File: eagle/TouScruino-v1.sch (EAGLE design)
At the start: 42 parts, among them J1 AVR_ISP, Q1 8MHz, Q2 MMBT2222A, Q3 8MHz, U1 ATMEGA1284P, U2 PJ28004C, U3 ARDUINO_SHIELD, U4 MCP73831, U5 MIC5209-3.3YS, X1 USBSMD

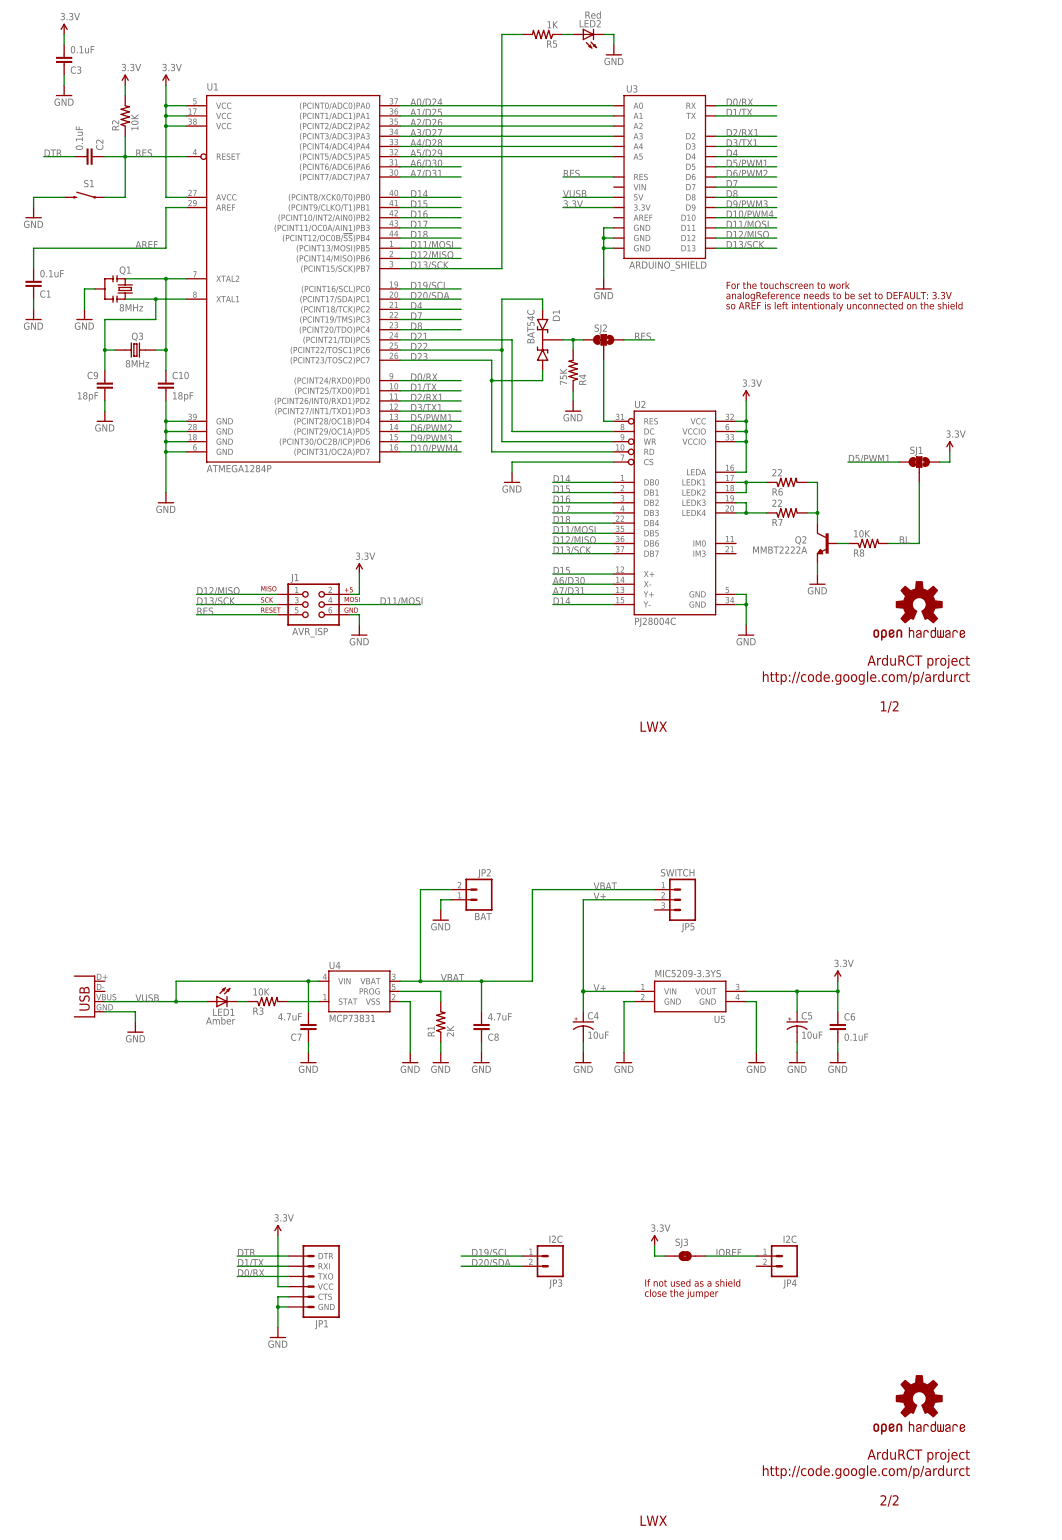
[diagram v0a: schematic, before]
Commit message: 
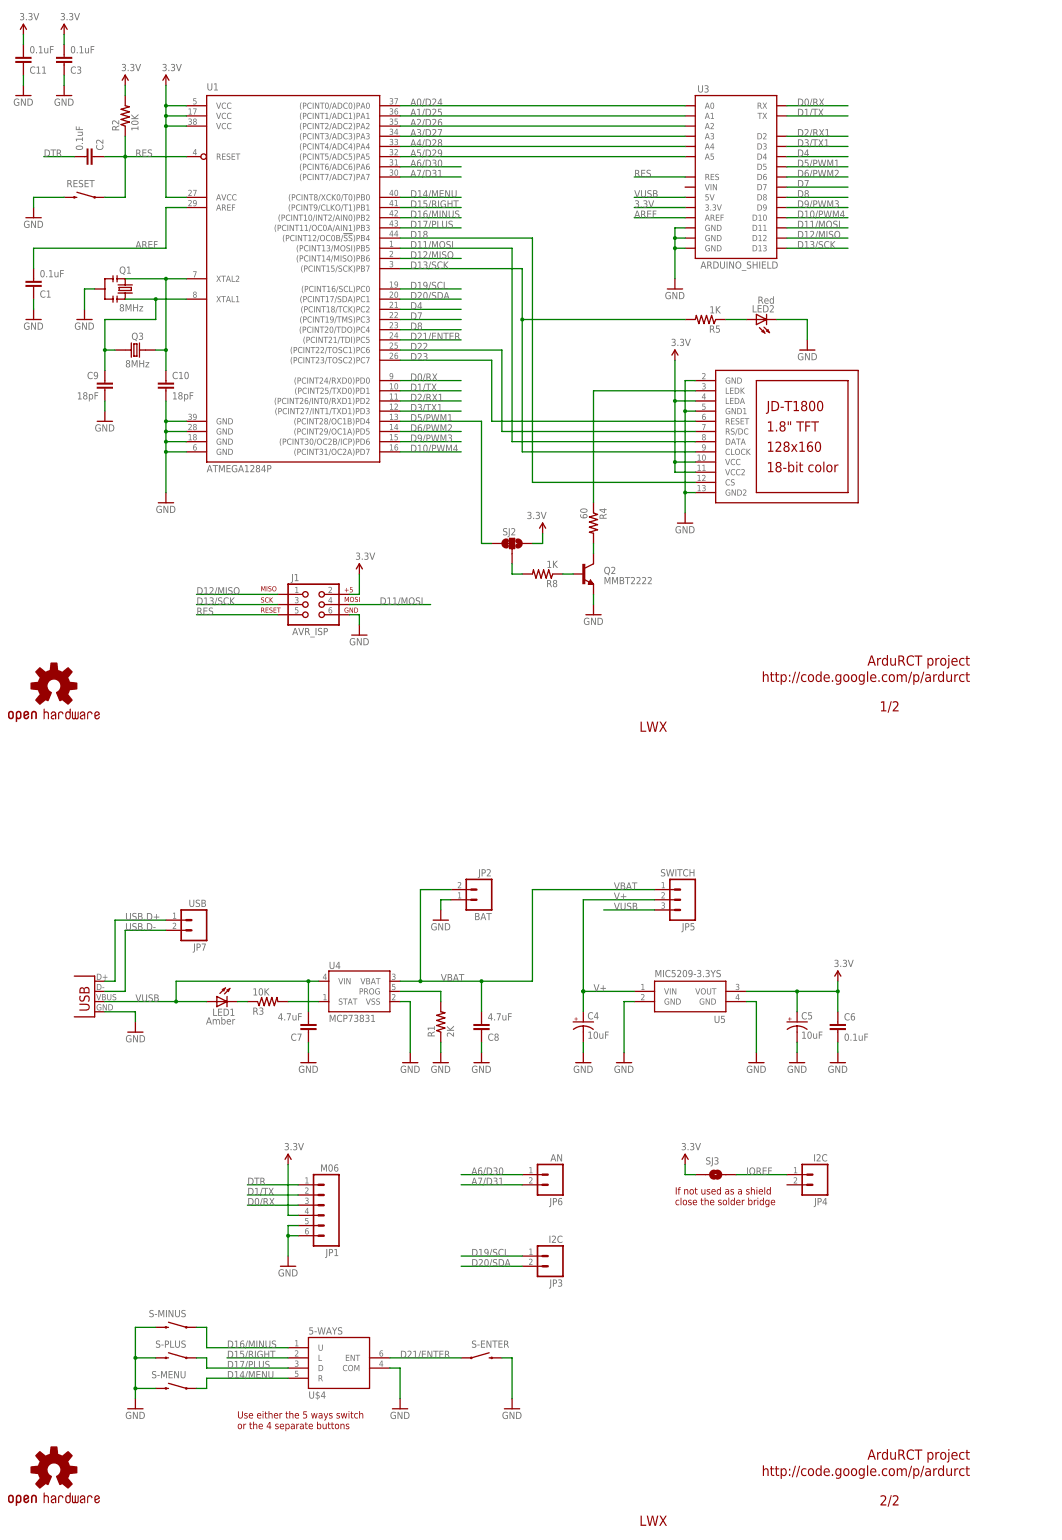
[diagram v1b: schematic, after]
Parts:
- removed D1: BAT54C, wibauxl:BAT54C
- removed R6, R7: 22, SparkFun:RESISTOR0805-RES
- removed SJ1: SJ_2WAYS_1-2, wibauxl:SJ_2WAYS_1-2
- removed U2: PJ28004C, wibauxl:PJ28004C
- added C11: 0.1uF, SparkFun:CAP0805
- added JP6: AN, wibauxl:M02
- added JP7: USB, wibauxl:M02
- added LCD1: JD-T1800, adafruit:JD-T1800
- added S-ENTER, S-MENU, S-MINUS, S-PLUS: SWITCH_SMD, wibauxl:SWITCH_SMD
- added U$4: 5-WAYS, wibauxl:5-WAYS
- JP1: value (none) -> M06; device SparkFun:ARDUINO_SERIAL_PROGRAMPTH -> wibauxl:M06
- Q2: value MMBT2222A -> MMBT2222
- R4: value 75K -> 60
- R8: value 10K -> 1K
- renumbered S1 to RESET
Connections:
- removed net BL: R8.2, SJ1.2
- removed net D14: U1.(PCINT8/XCK0/T0)PB0, U2.DB0, U2.Y-
- removed net D15: U1.(PCINT9/CLKO/T1)PB1, U2.DB1, U2.X+
- removed net D16: U1.(PCINT10/INT2/AIN0)PB2, U2.DB2
- removed net D17: U1.(PCINT11/OC0A/AIN1)PB3, U2.DB3
- removed net D21: U1.(PCINT21/TDI)PC5, U2.DC
- removed net LCD_RES: SJ2.2, U2.RES
- removed net N$25: R7.1, U2.LEDK3, U2.LEDK4
- removed net N$32: R6.1, U2.LEDK1, U2.LEDK2
- removed net N$7: Q2.C, R6.2, R7.2
- removed net N$9: D1.K, R4.2, SJ2.1
- new net BL_CMD: R8.2, SJ2.2
- new net D14/MENU: S-MENU.1, U$4.R, U1.(PCINT8/XCK0/T0)PB0
- new net D15/RIGHT: U$4.L, U1.(PCINT9/CLKO/T1)PB1
- new net D16/MINUS: S-MINUS.1, U$4.U, U1.(PCINT10/INT2/AIN0)PB2
- new net D17/PLUS: S-PLUS.1, U$4.D, U1.(PCINT11/OC0A/AIN1)PB3
- new net D21/ENTER: S-ENTER.1, U$4.ENT, U1.(PCINT21/TDI)PC5
- new net N$17: Q2.C, R4.2
- new net N$3: LCD1.LEDK, R4.1
- new net USB.D+: JP7.1, X1.D+
- new net USB.D-: JP7.2, X1.D-
- net 3.3V: now also C11.2, JP1.4, LCD1.LEDA, LCD1.VCC, LCD1.VCC2, SJ2.3; no longer JP1.VCC, SJ1.3, U2.LEDA, U2.VCC, U2.VCCIO@1, U2.VCCIO@2
- net A6/D30: now also JP6.1; no longer U2.X-
- net A7/D31: now also JP6.2; no longer U2.Y+
- net AREF: now also U3.AREF
- net D0/RX: now also JP1.3; no longer JP1.TXO
- net D1/TX: now also JP1.2; no longer JP1.RXI
- net D11/MOSI: now also LCD1.DATA; no longer U2.DB5
- net D12/MISO: no longer U2.DB6
- net D13/SCK: now also LCD1.CLOCK; no longer U2.DB7
- net D18: now also LCD1.CS; no longer U2.DB4
- net D22: now also LCD1.RS/DC; no longer D1.A2, U2.WR
- net D23: now also LCD1.RESET; no longer D1.A1, U2.RD
- net D5/PWM1: now also SJ2.1; no longer SJ1.1
- net DTR: now also JP1.1; no longer JP1.DTR
- net GND: now also C11.1, JP1.5, JP1.6, LCD1.GND, LCD1.GND1, LCD1.GND2, S-ENTER.2, S-MENU.2, S-MINUS.2, S-PLUS.2, U$4.COM; no longer JP1.CTS, JP1.GND, R4.1, U2.CS, U2.GND@1, U2.GND@2
- net RES: no longer SJ2.3
- net VUSB: now also JP5.3
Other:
- note added: "If not used as a shield close the solder bridge"
- note added: "Use either the 5 ways switch or the 4 separate buttons"
- note removed: "For the touchscreen to work"
- note removed: "If not used as a shield"
- note removed: "analogReference needs to be set to DEFAULT: 3.3V"
- note removed: "close the jumper"
- note removed: "so AREF is left intentionaly unconnected on the shield"
- moved on the sheet: JP1, JP4, LED2, Q2, R4, R5, R8, SJ2, SJ3, U3

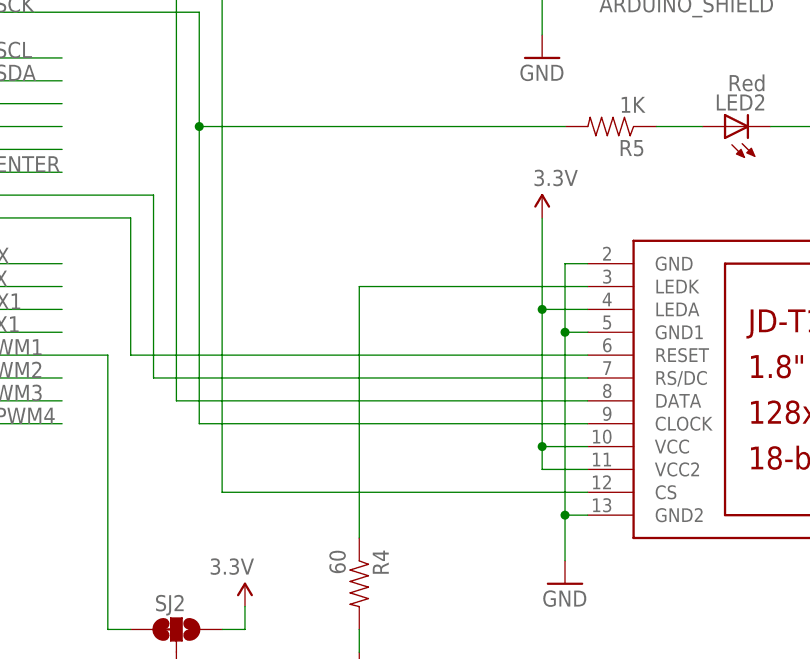
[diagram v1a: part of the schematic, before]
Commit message: 
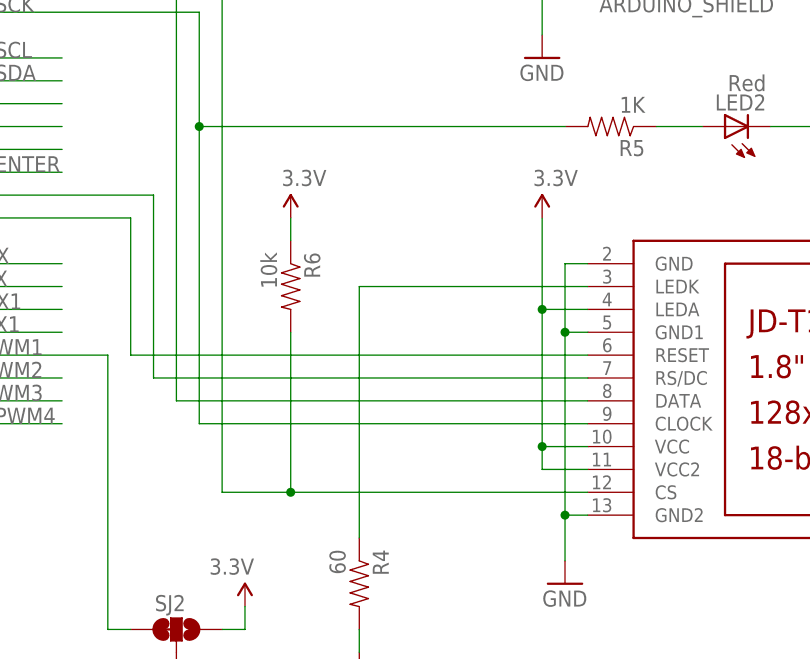
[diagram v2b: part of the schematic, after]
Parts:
- added R6: 10k, SparkFun:RESISTOR0805-RES
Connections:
- net 3.3V: now also R6.1
- net D18: now also R6.2
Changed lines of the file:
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@@
 <part name="GND22" library="SparkFun" deviceset="GND" device=""/>
 <part name="P+5" library="SparkFun" deviceset="3.3V" device=""/>
+<part name="R6" library="SparkFun" deviceset="RESISTOR" device="0805-RES" value="10k"/>
+<part name="P+9" library="SparkFun" deviceset="3.3V" device=""/>
 </parts>
 <sheets>
@@
 <instance part="GND22" gate="1" x="7.62" y="160.02"/>
 <instance part="P+5" gate="G$1" x="7.62" y="175.26"/>
+<instance part="R6" gate="G$1" x="142.24" y="86.36" rot="R270"/>
+<instance part="P+9" gate="G$1" x="142.24" y="93.98"/>
 </instances>
 <busses>
@@
 <pinref part="P+5" gate="G$1" pin="3.3V"/>
 </segment>
+<segment>
+<pinref part="P+9" gate="G$1" pin="3.3V"/>
+<pinref part="R6" gate="G$1" pin="1"/>
+<wire x1="142.24" y1="93.98" x2="142.24" y2="91.44" width="0.1524" layer="91"/>
+</segment>
 </net>
 <net name="D0/RX" class="0">
@@
 <wire x1="134.62" y1="124.46" x2="134.62" y2="63.5" width="0.1524" layer="91"/>
 <pinref part="LCD1" gate="G$1" pin="CS"/>
-<wire x1="134.62" y1="63.5" x2="175.26" y2="63.5" width="0.1524" layer="91"/>
-</segment>
-</net>
+<wire x1="134.62" y1="63.5" x2="142.24" y2="63.5" width="0.1524" layer="91"/>
+<pinref part="R6" gate="G$1" pin="2"/>
+<wire x1="142.24" y1="63.5" x2="175.26" y2="63.5" width="0.1524" layer="91"/>
+<wire x1="142.24" y1="81.28" x2="142.24" y2="63.5" width="0.1524" layer="91"/>
+<junction x="142.24" y="63.5"/>
+</segment>
+</net>
